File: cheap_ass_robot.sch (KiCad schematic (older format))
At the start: 43 parts, among them IC1 MC34063A, IC2 ATMEGA328P-AU-R, IC3 FT232RL, IC4 L293DD, J1 USB_B, J2 DIGITAL 2, J3 ANALOG IN, J4 POWER, J5 DIGITAL 1, M1 Motor_DC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

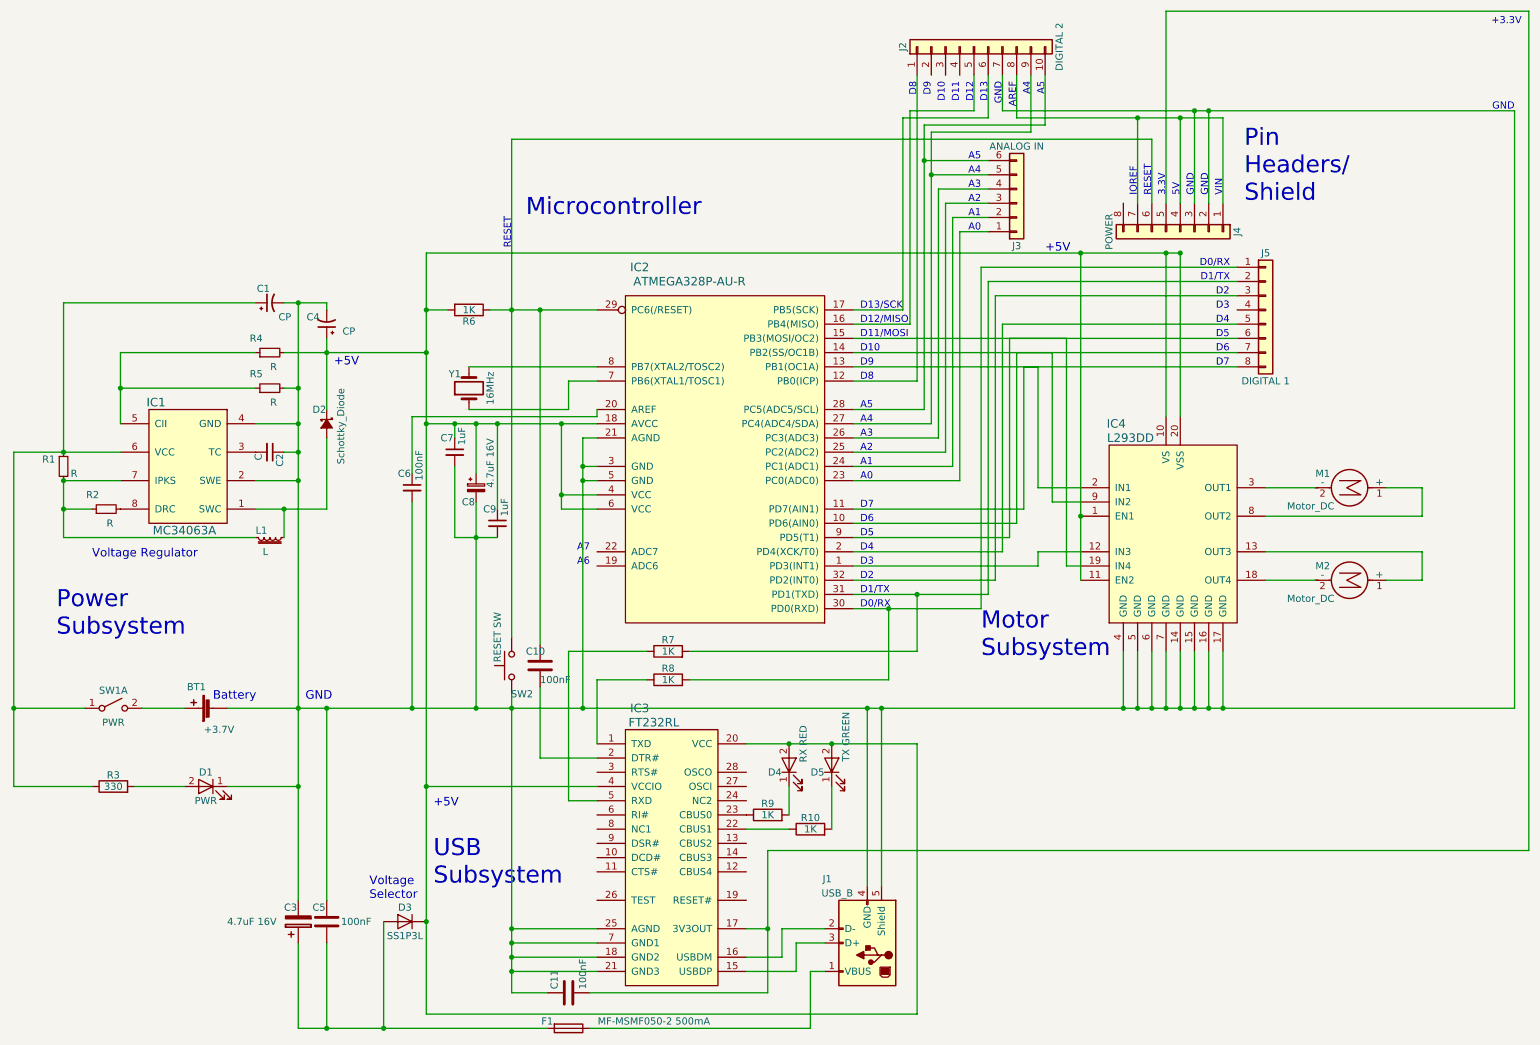
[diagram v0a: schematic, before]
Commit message: fixed diagram level electrical issues and added caps from xtal to gnd
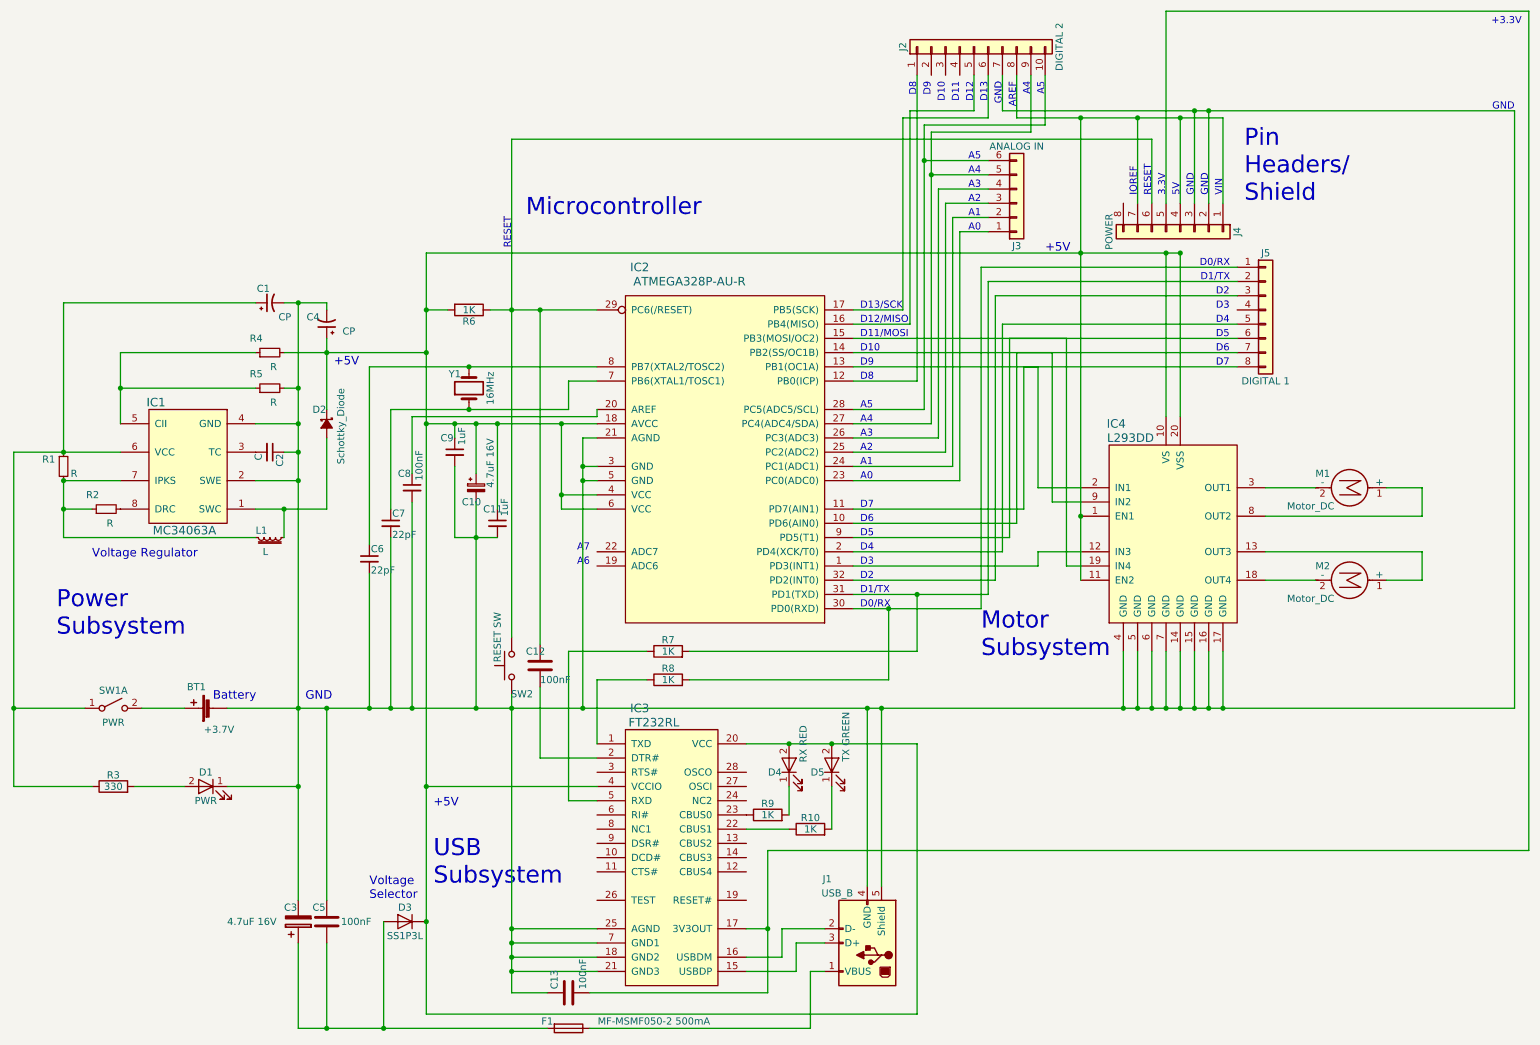
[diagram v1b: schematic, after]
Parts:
- added C6, C7: 22pF, Capacitors_SMD:C_0805, symbol C_Small
- renumbered C8 to C10, C9 to C11, C10 to C12, C11 to C13, C6 to C8, C7 to C9
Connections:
- net at BT1.2 (-), C1.2, C10.2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: now also C6.2, C7.2
- net at C10.1, C11.1, C4.1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: now also J2.8 (Pin_8), J4.1 (Pin_1), J4.4 (Pin_4), J4.7 (Pin_7)
- net at IC2.7 (PB6(XTAL1/TOSC1)), Y1.1: now also C7.1
- net at IC2.8 (PB7(XTAL2/TOSC2)), Y1.2: now also C6.1
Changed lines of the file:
@@
 Battery
 $Comp
-L C C10
+L C C12
 U 1 1 5B6296E1
 P 4200 5150
-F 0 "C10" H 4100 5250 50  0000 L CNN
+F 0 "C12" H 4100 5250 50  0000 L CNN
 F 1 "100nF" H 4200 5050 50  0000 L CNN
 F 2 "Capacitors_SMD:C_0805" H 4238 5000 50  0001 C CNN
@@
 $EndComp
 $Comp
-L C C11
+L C C13
 U 1 1 5B62DCDA
 P 4400 7450
-F 0 "C11" H 4425 7550 50  0000 L CNN
+F 0 "C13" H 4425 7550 50  0000 L CNN
 F 1 "100nF" H 4425 7350 50  0000 L CNN
 F 2 "Capacitors_SMD:C_0805" H 4438 7300 50  0001 C CNN
@@
 $EndComp
 $Comp
-L C_Small C7
+L C_Small C9
 U 1 1 5B63D83F
 P 3600 3650
-F 0 "C7" H 3500 3750 50  0000 L CNN
+F 0 "C9" H 3500 3750 50  0000 L CNN
 F 1 "1uF" V 3650 3700 50  0000 L CNN
 F 2 "Capacitors_SMD:C_0805" H 3600 3650 50  0001 C CNN
@@
 $EndComp
 $Comp
-L CP_Small C8
+L CP_Small C10
 U 1 1 5B63D8E0
 P 3750 3900
-F 0 "C8" H 3650 3800 50  0000 L CNN
+F 0 "C10" H 3650 3800 50  0000 L CNN
 F 1 "4.7uF 16V" V 3850 3900 50  0000 L CNN
 F 2 "Capacitors_SMD:CP_Elec_4x5.7" H 3750 3900 50  0001 C CNN
@@
 $EndComp
 $Comp
-L C_Small C9
+L C_Small C11
 U 1 1 5B63DA64
 P 3900 4150
-F 0 "C9" H 3800 4250 50  0000 L CNN
+F 0 "C11" H 3800 4250 50  0000 L CNN
 F 1 "1uF" V 3950 4200 50  0000 L CNN
 F 2 "Capacitors_SMD:C_0805" H 3900 4150 50  0001 C CNN
@@
 $EndComp
 $Comp
-L C_Small C6
+L C_Small C8
 U 1 1 5B63F1E8
 P 3300 3900
-F 0 "C6" H 3200 4000 50  0000 L CNN
+F 0 "C8" H 3200 4000 50  0000 L CNN
 F 1 "100nF" V 3350 3950 50  0000 L CNN
 F 2 "Capacitors_SMD:C_0805" H 3300 3900 50  0001 C CNN
@@
 Connection ~ 8000 2250
 Wire Wire Line
-	8000 2250 8000 4550
+	8000 1300 8000 4550
 Wire Wire Line
 	7900 4450 8000 4450
@@
 	7100 3750 6400 3750
 Wire Wire Line
-	4600 3050 3700 3050
-Wire Wire Line
-	4400 3350 3700 3350
+	3000 3050 4600 3050
+Wire Wire Line
+	3150 3350 4400 3350
+$Comp
+L C_Small C7
+U 1 1 5B9B2225
+P 3150 4150
+F 0 "C7" H 3160 4220 50  0000 L CNN
+F 1 "22pF" H 3160 4070 50  0000 L CNN
+F 2 "Capacitors_SMD:C_0805" H 3150 4150 50  0001 C CNN
+F 3 "" H 3150 4150 50  0001 C CNN
+	1    3150 4150
+	1    0    0    -1
+$EndComp
+$Comp
+L C_Small C6
+U 1 1 5B9B22F5
+P 3000 4400
+F 0 "C6" H 3010 4470 50  0000 L CNN
+F 1 "22pF" H 3010 4320 50  0000 L CNN
+F 2 "Capacitors_SMD:C_0805" H 3000 4400 50  0001 C CNN
+F 3 "" H 3000 4400 50  0001 C CNN
+	1    3000 4400
+	1    0    0    -1
+$EndComp
+Wire Wire Line
+	3150 3350 3150 4050
+Connection ~ 3700 3350
+Wire Wire Line
+	3150 4250 3150 5450
+Connection ~ 3150 5450
+Wire Wire Line
+	3000 3050 3000 4300
+Connection ~ 3700 3050
+Wire Wire Line
+	3000 4500 3000 5450
+Connection ~ 3000 5450
+Connection ~ 8000 1300
 $EndSCHEMATC

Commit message: will probably be revision alpha-1
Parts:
- C4: footprint Capacitors_SMD:CP_Elec_4x5.7 -> Capacitors_SMD:CP_Elec_6.3x7.7
- D2, D3: footprint Diodes_SMD:D_SMB -> Diodes_SMD:D_SOD-123F
- L1: footprint Inductors_SMD:L_1210 -> Inductors_SMD:L_0805
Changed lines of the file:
@@
 EESchema Schematic File Version 2
+LIBS:cheap_ass_robot-rescue
 LIBS:power
 LIBS:device
@@
 F 0 "L1" V 2250 4150 50  0000 L CNN
 F 1 "L" V 2400 4200 50  0000 L CNN
-F 2 "Inductors_SMD:L_1210" H 2300 4250 50  0001 C CNN
+F 2 "Inductors_SMD:L_0805" H 2300 4250 50  0001 C CNN
 F 3 "" H 2300 4250 50  0001 C CNN
 	1    2300 4250
@@
 F 0 "D2" V 2600 3350 50  0000 L CNN
 F 1 "Schottky_Diode" H 2450 3550 50  0000 L CNN
-F 2 "Diodes_SMD:D_SMB" V 2700 3450 50  0001 C CNN
+F 2 "Diodes_SMD:D_SOD-123F" V 2700 3450 50  0001 C CNN
 F 3 "" V 2700 3450 50  0001 C CNN
 	1    2700 3450
@@
 F 0 "C4" H 2750 2700 50  0000 L CNN
 F 1 "CP" H 2500 2800 50  0000 L CNN
-F 2 "Capacitors_SMD:CP_Elec_4x5.7" H 2700 2750 50  0001 C CNN
+F 2 "Capacitors_SMD:CP_Elec_6.3x7.7" H 2700 2750 50  0001 C CNN
 F 3 "" H 2700 2750 50  0001 C CNN
 	1    2700 2750
@@
 F 0 "D3" H 3250 7050 50  0000 C CNN
 F 1 "SS1P3L" H 3250 6850 50  0000 C CNN
-F 2 "Diodes_SMD:D_SMB" H 3250 6950 50  0001 C CNN
+F 2 "Diodes_SMD:D_SOD-123F" H 3250 6950 50  0001 C CNN
 F 3 "" H 3250 6950 50  0001 C CNN
 	1    3250 6950

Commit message: sync; most recent change was fixing missed connection to ground on ftdi chip
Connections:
- net at BT1.2 (-), C1.2, C10.2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: now also IC3.26 (TEST)
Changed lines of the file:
@@
 Connection ~ 3000 5450
 Connection ~ 8000 1300
+Wire Wire Line
+	4600 6800 4000 6800
+Connection ~ 4000 6800
 $EndSCHEMATC

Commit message: all out war against heat
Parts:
- removed L1: L, Inductors_SMD:L_0805, symbol L_Core_Iron_Small
- added L1, L2, L3: L, Inductors_SMD:L_0805, symbol L
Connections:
- net at D2.2 (A), IC1.1 (SWC): now also L3.1
- net at IC1.7 (IPKS), R1.2, R2.1: now also L1.2
- new net: L1.1, L2.2
- new net: L2.1, L3.2
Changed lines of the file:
@@
-$EndComp
-$Comp
-L L_Core_Iron_Small L1
-U 1 1 5B613419
-P 2300 4250
-F 0 "L1" V 2250 4150 50  0000 L CNN
-F 1 "L" V 2400 4200 50  0000 L CNN
-F 2 "Inductors_SMD:L_0805" H 2300 4250 50  0001 C CNN
-F 3 "" H 2300 4250 50  0001 C CNN
-	1    2300 4250
-	0    1    1    0
 $EndComp
 $Comp
@@
 Text Notes 6450 3350 0    50   ~ 0
 A5
-Text Notes 1050 4400 0    60   ~ 0
+Text Notes 1400 4600 0    60   ~ 0
 Voltage Regulator
 Text Notes 1900 5400 0    60   ~ 0
@@
 Connection ~ 2400 4050
 Wire Wire Line
-	2400 4250 2400 4050
+	2400 4050 2400 4400
 Wire Wire Line
 	2400 3200 2500 3200
@@
 Connection ~ 850  4050
 Wire Wire Line
-	850  4250 2200 4250
-Wire Wire Line
-	850  3850 850  4250
+	850  3850 850  4400
 Wire Wire Line
 	850  3850 1250 3850
@@
 	4600 6800 4000 6800
 Connection ~ 4000 6800
+$Comp
+L L L1
+U 1 1 5CD67618
+P 1150 4400
+F 0 "L1" V 1100 4400 50  0000 C CNN
+F 1 "L" V 1225 4400 50  0000 C CNN
+F 2 "Inductors_SMD:L_0805" H 1150 4400 50  0001 C CNN
+F 3 "" H 1150 4400 50  0001 C CNN
+	1    1150 4400
+	0    1    1    0
+$EndComp
+$Comp
+L L L2
+U 1 1 5CD67719
+P 1650 4400
+F 0 "L2" V 1600 4400 50  0000 C CNN
+F 1 "L" V 1725 4400 50  0000 C CNN
+F 2 "Inductors_SMD:L_0805" H 1650 4400 50  0001 C CNN
+F 3 "" H 1650 4400 50  0001 C CNN
+	1    1650 4400
+	0    1    1    0
+$EndComp
+$Comp
+L L L3
+U 1 1 5CD677C7
+P 2150 4400
+F 0 "L3" V 2100 4400 50  0000 C CNN
+F 1 "L" V 2225 4400 50  0000 C CNN
+F 2 "Inductors_SMD:L_0805" H 2150 4400 50  0001 C CNN
+F 3 "" H 2150 4400 50  0001 C CNN
+	1    2150 4400
+	0    1    1    0
+$EndComp
+Wire Wire Line
+	850  4400 1000 4400
+Wire Wire Line
+	1300 4400 1500 4400
+Wire Wire Line
+	1800 4400 2000 4400
+Wire Wire Line
+	2400 4400 2300 4400
 $EndSCHEMATC
